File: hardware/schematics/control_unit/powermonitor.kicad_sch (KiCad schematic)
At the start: 10 parts, among them T1 Transformer_1P_1S, U18 LM324

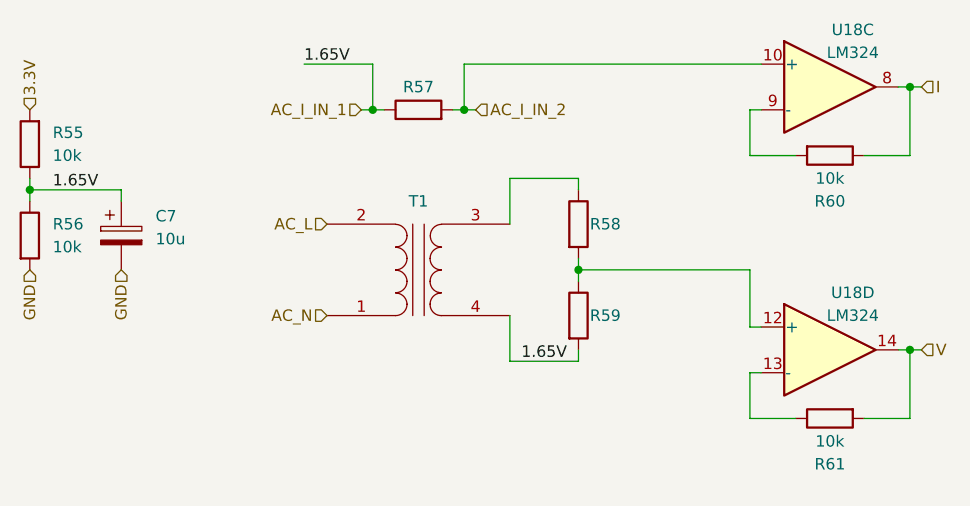
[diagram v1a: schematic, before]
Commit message: feat: added PowerMonitor resistor's values.
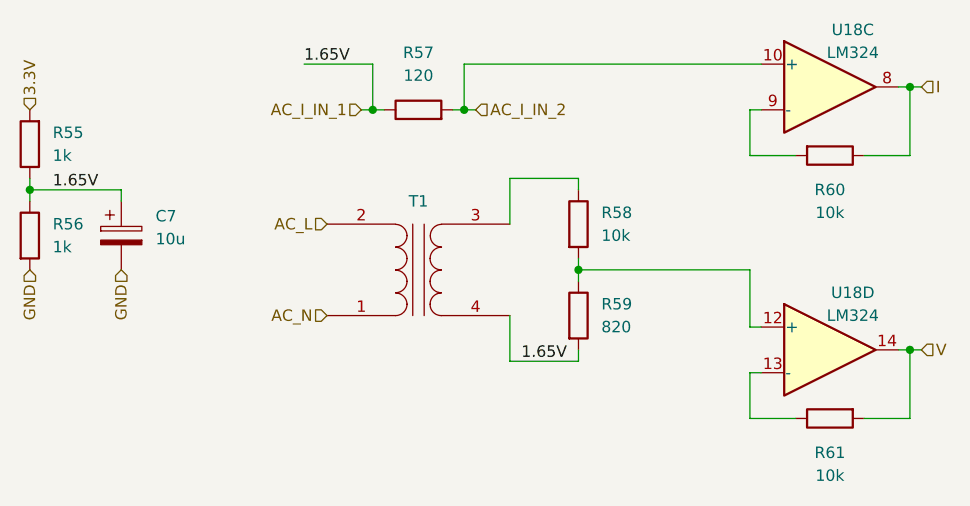
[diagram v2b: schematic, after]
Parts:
- R55, R56: value 10k -> 1k
- R57: value R -> 120
- R58: value R -> 10k
- R59: value R -> 820
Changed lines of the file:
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@@
 		(dnp no)
 		(property "Reference" "R61"
-			(at 190.5 121.92 90)
+			(at 190.5 120.65 90)
 			(effects
 				(font
@@
 		)
 		(property "Value" "10k"
-			(at 190.5 119.38 90)
+			(at 190.5 123.19 90)
 			(effects
 				(font
@@
 		(dnp no)
 		(property "Reference" "R57"
-			(at 144.78 80.01 90)
-			(effects
-				(font
-					(size 1.27 1.27)
-				)
-			)
-		)
-		(property "Value" "R"
-			(at 144.78 80.01 90)
-			(effects
-				(font
-					(size 1.27 1.27)
-				)
-				(hide yes)
+			(at 144.78 76.2 90)
+			(effects
+				(font
+					(size 1.27 1.27)
+				)
+			)
+		)
+		(property "Value" "120"
+			(at 144.78 78.74 90)
+			(effects
+				(font
+					(size 1.27 1.27)
+				)
 			)
 		)
@@
 		(dnp no)
 		(property "Reference" "R60"
-			(at 190.5 92.71 90)
+			(at 190.5 91.44 90)
 			(effects
 				(font
@@
 		)
 		(property "Value" "10k"
-			(at 190.5 90.17 90)
+			(at 190.5 93.98 90)
 			(effects
 				(font
@@
 		(dnp no)
 		(property "Reference" "R59"
-			(at 163.83 105.41 0)
-			(effects
-				(font
-					(size 1.27 1.27)
-				)
-				(justify left)
-			)
-		)
-		(property "Value" "R"
+			(at 165.1 104.14 0)
+			(effects
+				(font
+					(size 1.27 1.27)
+				)
+				(justify left)
+			)
+		)
+		(property "Value" "820"
 			(at 165.1 106.6799 0)
 			(effects
@@
 				)
 				(justify left)
-				(hide yes)
 			)
 		)
@@
 		(dnp no)
 		(property "Reference" "R58"
-			(at 163.83 95.25 0)
-			(effects
-				(font
-					(size 1.27 1.27)
-				)
-				(justify left)
-			)
-		)
-		(property "Value" "R"
+			(at 165.1 93.98 0)
+			(effects
+				(font
+					(size 1.27 1.27)
+				)
+				(justify left)
+			)
+		)
+		(property "Value" "10k"
 			(at 165.1 96.5199 0)
 			(effects
@@
 				)
 				(justify left)
-				(hide yes)
 			)
 		)
@@
 			)
 		)
-		(property "Value" "10k"
+		(property "Value" "1k"
 			(at 104.14 97.7899 0)
 			(effects
@@
 			)
 		)
-		(property "Value" "10k"
+		(property "Value" "1k"
 			(at 104.14 87.6299 0)
 			(effects

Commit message: fix
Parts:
- T1: footprint HomeMonitor:Transformer -> PowerMonitor:Transformer
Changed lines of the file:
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@@
 			)
 		)
-		(property "Footprint" "HomeMonitor:Transformer"
+		(property "Footprint" "PowerMonitor:Transformer"
 			(at 144.78 100.33 0)
 			(effects

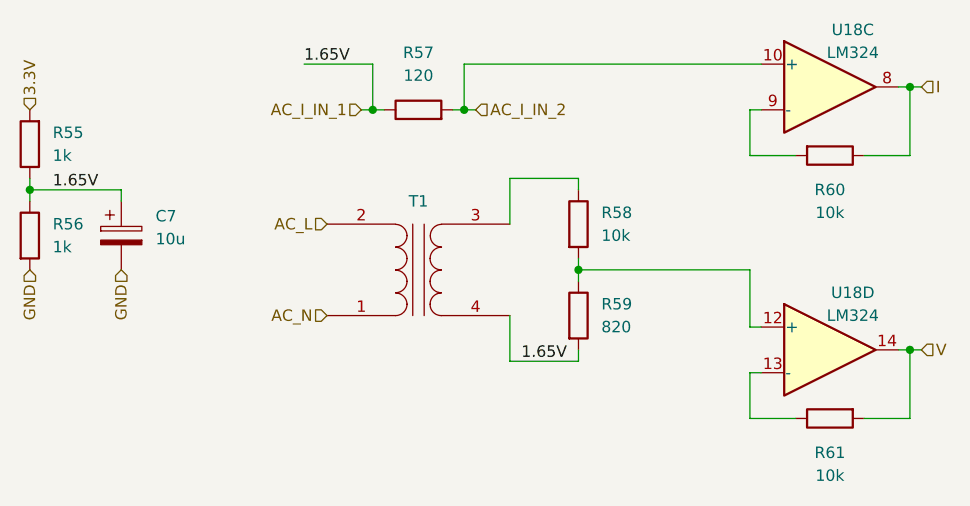
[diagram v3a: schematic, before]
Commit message: fix: powermonitor lower resistor to 680ohm
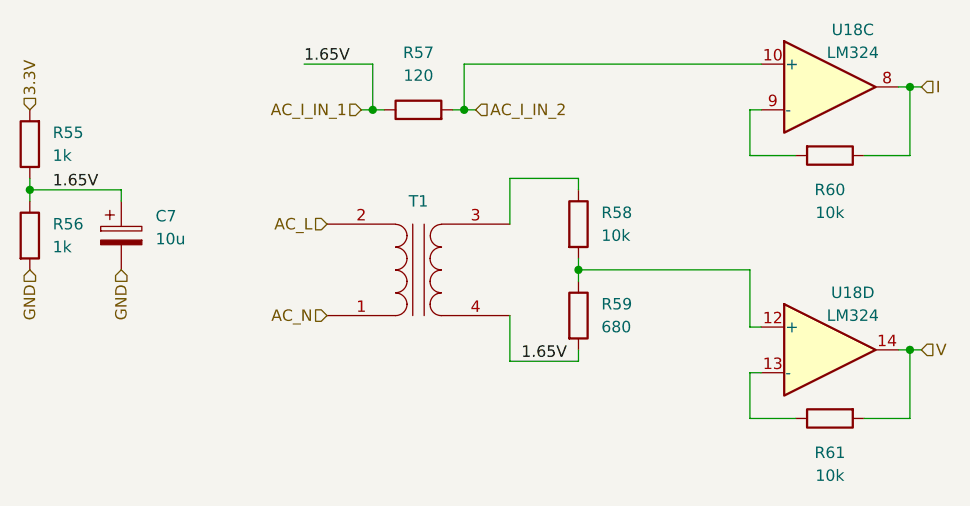
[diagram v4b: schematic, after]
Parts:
- R59: value 820 -> 680
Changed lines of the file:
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@@
 			)
 		)
-		(property "Value" "820"
+		(property "Value" "680"
 			(at 165.1 106.6799 0)
 			(effects
